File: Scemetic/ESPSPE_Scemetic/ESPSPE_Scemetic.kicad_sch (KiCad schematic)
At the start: 53 parts, among them J1 Screw_Terminal_01x02, J2 Conn_01x01_Pin, SW1 RESET, T1 749070010, U1 DEVKIT_V1_ESP32-WROOM-32, U2 ADIN1110, U3 TVS_Diode_8240136, Y2 CFPX-180_830105863709

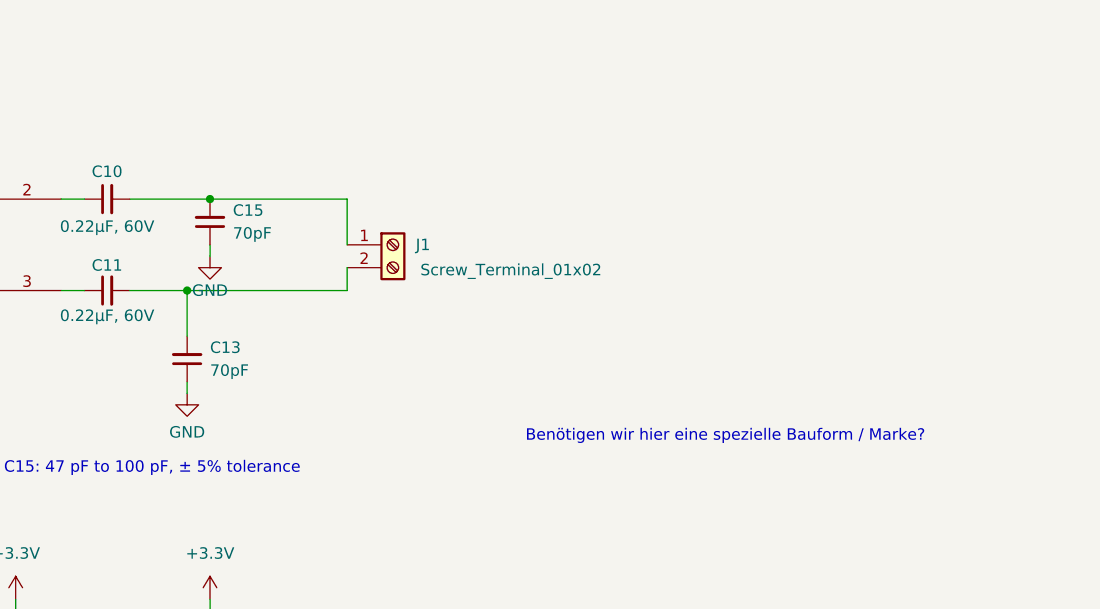
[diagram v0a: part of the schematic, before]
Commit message: Vias eingefügt
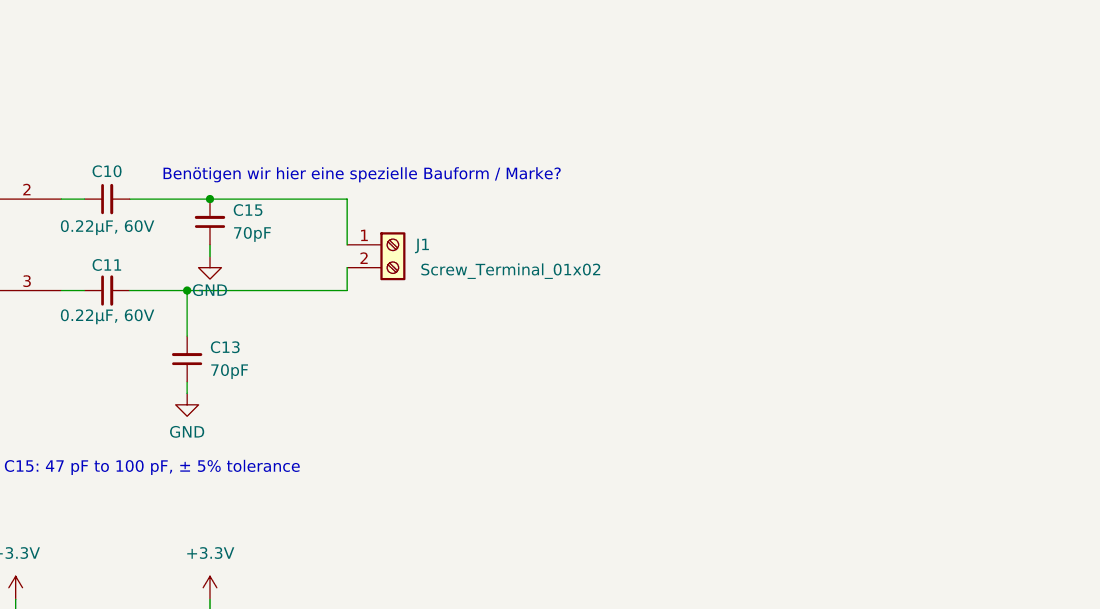
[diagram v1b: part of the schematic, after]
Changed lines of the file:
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@@
 	(text "Benötigen wir hier eine spezielle Bauform / Marke? "
 		(exclude_from_sim no)
-		(at 272.542 68.834 0)
+		(at 232.156 39.878 0)
 		(effects
 			(font

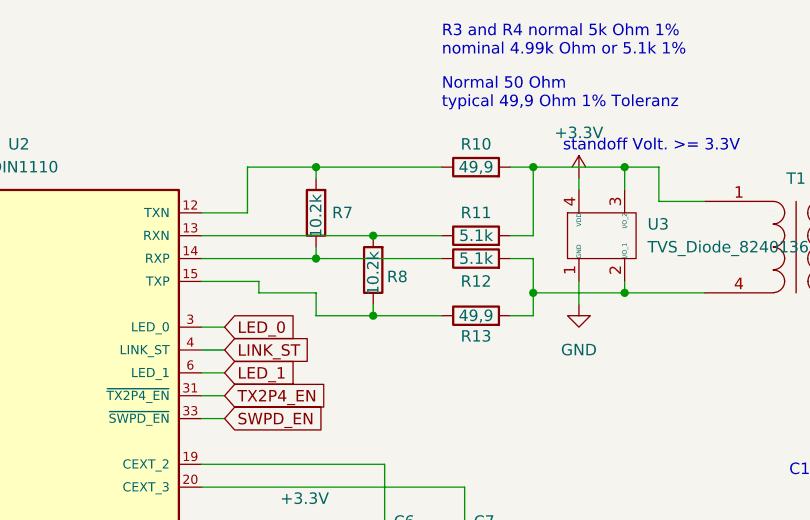
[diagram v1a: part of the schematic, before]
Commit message: Bestellliste erstellt, Schaltplanänderung angepasst.
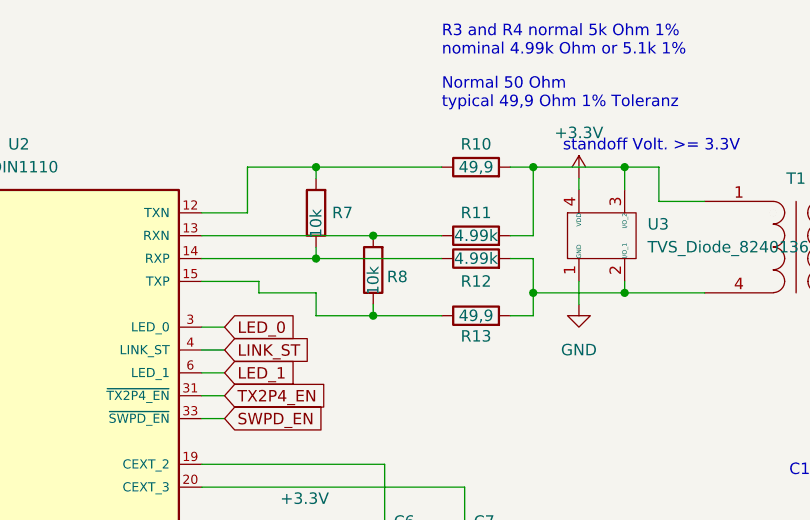
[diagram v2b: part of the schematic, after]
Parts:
- R10, R13: footprint Resistor_SMD:R_0805_2012Metric_Pad1.20x1.40mm_HandSolder -> Resistor_SMD:R_0603_1608Metric_Pad0.98x0.95mm_HandSolder
- R11, R12: value 5.1k -> 4.99k; footprint Resistor_SMD:R_0805_2012Metric_Pad1.20x1.40mm_HandSolder -> Resistor_SMD:R_0603_1608Metric_Pad0.98x0.95mm_HandSolder
- R7, R8: value 10.2k -> 10k
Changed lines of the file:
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@@
 			)
 		)
-		(property "Value" "10.2k"
+		(property "Value" "10k"
 			(at 163.83 53.594 90)
 			(effects
@@
 			)
 		)
-		(property "Footprint" "Resistor_SMD:R_0805_2012Metric_Pad1.20x1.40mm_HandSolder"
+		(property "Footprint" "Resistor_SMD:R_0603_1608Metric_Pad0.98x0.95mm_HandSolder"
 			(at 175.26 41.148 90)
 			(effects
@@
 			)
 		)
-		(property "Value" "5.1k"
+		(property "Value" "4.99k"
 			(at 175.26 46.99 90)
 			(effects
@@
 			)
 		)
-		(property "Footprint" "Resistor_SMD:R_0805_2012Metric_Pad1.20x1.40mm_HandSolder"
+		(property "Footprint" "Resistor_SMD:R_0603_1608Metric_Pad0.98x0.95mm_HandSolder"
 			(at 175.26 48.768 90)
 			(effects
@@
 			)
 		)
-		(property "Footprint" "Resistor_SMD:R_0805_2012Metric_Pad1.20x1.40mm_HandSolder"
+		(property "Footprint" "Resistor_SMD:R_0603_1608Metric_Pad0.98x0.95mm_HandSolder"
 			(at 175.26 57.658 90)
 			(effects
@@
 			)
 		)
-		(property "Value" "10.2k"
+		(property "Value" "10k"
 			(at 157.48 47.244 90)
 			(effects
@@
 			)
 		)
-		(property "Value" "5.1k"
+		(property "Value" "4.99k"
 			(at 175.26 49.53 90)
 			(effects
@@
 			)
 		)
-		(property "Footprint" "Resistor_SMD:R_0805_2012Metric_Pad1.20x1.40mm_HandSolder"
+		(property "Footprint" "Resistor_SMD:R_0603_1608Metric_Pad0.98x0.95mm_HandSolder"
 			(at 175.26 51.308 90)
 			(effects
